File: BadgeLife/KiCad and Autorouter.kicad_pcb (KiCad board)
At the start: 2 copper layers, 30 x 30 mm, 21 parts, among them SW1 Power, SW2 Dice Roll, U1 ATtiny85

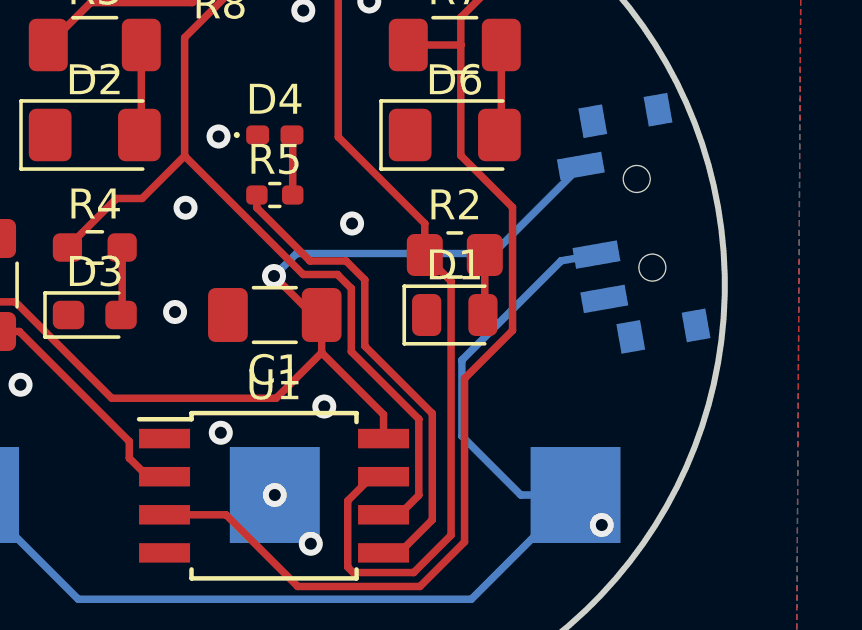
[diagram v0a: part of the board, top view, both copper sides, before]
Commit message: HtmlBom Generated and one footprint corrected
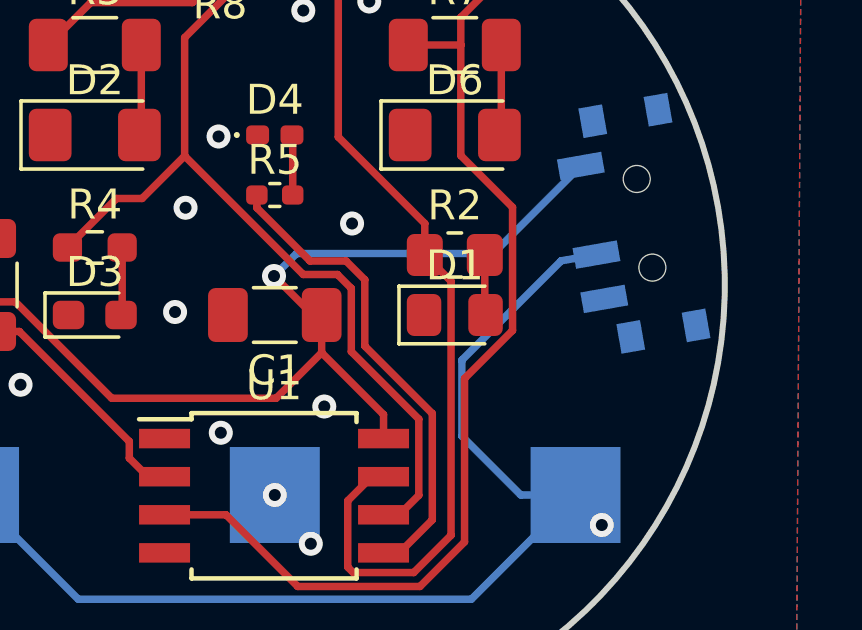
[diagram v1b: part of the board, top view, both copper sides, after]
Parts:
- D1: footprint Diode_SMD:D_0805_2012Metric -> Diode_SMD:D_0805_2012Metric_Pad1.15x1.40mm_HandSolder
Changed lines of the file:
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@@
     )
   )
-  (footprint "Diode_SMD:D_0805_2012Metric" (layer "F.Cu")
+  (footprint "Diode_SMD:D_0805_2012Metric_Pad1.15x1.40mm_HandSolder" (layer "F.Cu")
     (at 106 51)
     (descr "Diode SMD 0805 (2012 Metric), square (rectangular) end terminal, IPC_7351 nominal, (Body size source: https://docs.google.com/spreadsheets/d/1BsfQQcO9C6DZCsRaXUlFlo91Tg2WpOkGARC1WS5S8t0/edit?usp=sharing), generated with kicad-footprint-generator")
-    (tags "diode")
+    (tags "diode handsolder")
     (property "Sheetfile" "KiCad and Autorouter.kicad_sch")
     (property "Sheetname" "")
@@
       (effects (font (size 0.5 0.5) (thickness 0.08)))
     )
-    (fp_line (start -1.685 -0.96) (end -1.685 0.96) (layer "F.SilkS") (width 0.12))
-    (fp_line (start -1.685 0.96) (end 1 0.96) (layer "F.SilkS") (width 0.12))
-    (fp_line (start 1 -0.96) (end -1.685 -0.96) (layer "F.SilkS") (width 0.12))
-    (fp_line (start 1.68 -0.95) (end 1.68 0.95) (layer "F.CrtYd") (width 0.05))
-    (fp_line (start -1.68 -0.95) (end 1.68 -0.95) (layer "F.CrtYd") (width 0.05))
-    (fp_line (start 1.68 0.95) (end -1.68 0.95) (layer "F.CrtYd") (width 0.05))
-    (fp_line (start -1.68 0.95) (end -1.68 -0.95) (layer "F.CrtYd") (width 0.05))
+    (fp_line (start -1.86 -0.96) (end -1.86 0.96) (layer "F.SilkS") (width 0.12))
+    (fp_line (start 1 -0.96) (end -1.86 -0.96) (layer "F.SilkS") (width 0.12))
+    (fp_line (start -1.86 0.96) (end 1 0.96) (layer "F.SilkS") (width 0.12))
+    (fp_line (start -1.85 -0.95) (end 1.85 -0.95) (layer "F.CrtYd") (width 0.05))
+    (fp_line (start -1.85 0.95) (end -1.85 -0.95) (layer "F.CrtYd") (width 0.05))
+    (fp_line (start 1.85 0.95) (end -1.85 0.95) (layer "F.CrtYd") (width 0.05))
+    (fp_line (start 1.85 -0.95) (end 1.85 0.95) (layer "F.CrtYd") (width 0.05))
+    (fp_line (start -1 -0.3) (end -1 0.6) (layer "F.Fab") (width 0.1))
+    (fp_line (start 1 0.6) (end 1 -0.6) (layer "F.Fab") (width 0.1))
+    (fp_line (start 1 -0.6) (end -0.7 -0.6) (layer "F.Fab") (width 0.1))
     (fp_line (start -1 0.6) (end 1 0.6) (layer "F.Fab") (width 0.1))
     (fp_line (start -0.7 -0.6) (end -1 -0.3) (layer "F.Fab") (width 0.1))
-    (fp_line (start -1 -0.3) (end -1 0.6) (layer "F.Fab") (width 0.1))
-    (fp_line (start 1 -0.6) (end -0.7 -0.6) (layer "F.Fab") (width 0.1))
-    (fp_line (start 1 0.6) (end 1 -0.6) (layer "F.Fab") (width 0.1))
-    (pad "1" smd roundrect (at -0.9375 0) (size 0.975 1.4) (layers "F.Cu" "F.Paste" "F.Mask") (roundrect_rratio 0.25)
+    (pad "1" smd roundrect (at -1.025 0) (size 1.15 1.4) (layers "F.Cu" "F.Paste" "F.Mask") (roundrect_rratio 0.217391)
       (net 2 "GND") (pinfunction "K") (pintype "passive"))
-    (pad "2" smd roundrect (at 0.9375 0) (size 0.975 1.4) (layers "F.Cu" "F.Paste" "F.Mask") (roundrect_rratio 0.25)
+    (pad "2" smd roundrect (at 1.025 0) (size 1.15 1.4) (layers "F.Cu" "F.Paste" "F.Mask") (roundrect_rratio 0.217391)
       (net 4 "Net-(D1-Pad2)") (pinfunction "A") (pintype "passive"))
     (model "${KICAD6_3DMODEL_DIR}/Diode_SMD.3dshapes/D_0805_2012Metric.wrl"

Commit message: more small edits
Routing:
- net /LED_4: track 32.6 -> 34.2 mm
- net GND: track 0.00 -> 1.30 mm, vias 16 -> 11
- net /LED_6: track 55.1 -> 53.8 mm
- net +3V3: track 38.5 -> 39.1 mm
- net Net-(BT1-Pad1): vias 1 -> 0
